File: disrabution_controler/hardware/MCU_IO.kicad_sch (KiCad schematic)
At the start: 48 parts, among them J1 Conn_Coaxial, J2 PROG_PORT, J3 JTAG, Q17 NMOS, U2 ESP32-S2FH2, U3 ECMF02-2AMX6, U9 PI4IOE5V6416LEX, Y1 40 MHz

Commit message: more hardware work
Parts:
- removed R72: 10K, symbol Device:R
- removed R73: 20K, symbol Device:R
- removed TP26: ~, symbol Connector:TestPoint
- added C19, C20, C21, C22: 0uF1, symbol Device:C
- added C23, C24: 10UF, symbol Device:C
- added JP3: ~, symbol Jumper:SolderJumper_3_Open
- added R59, R85: 60R, symbol Device:R
- added U5: TJA1043T, Package_SO:SOIC-14_3.9x8.7mm_P1.27mm, symbol Interface_CAN_LIN:TJA1043T
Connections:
- net +12V: now also C22.1, C24.1, U5.10 (VBAT)
- net +3V3: now also C20.1, C21.1, C23.1, U5.3 (VCC), U5.5 (VIO)
- net CAN_H: now also R59.1, U5.13 (CANH)
- net CAN_L: now also R85.2, U5.12 (CANL)
- net DISRABUTION_NEO_PIXELS: now also U2.28 (GPIO21); no longer U2.37 (GPIO33)
- net GND: now also C19.2, C20.2, C21.2, C22.2, C23.2, C24.2, U5.2 (GND)
- net PERIPHERAL_PWR: now reaches J4.3
- net PERIPHERAL_PWR_GATE: now reaches U2.10 (GPIO5)
- net PERIPHERAL_PWR_CSN_DEV: now reaches U2.18 (GPIO13)
- net CAN_CS renamed CAN_STB
- net CAN_STB: now also U5.14 (~{STB})
- net CAN_INT renamed CAN_ERR
- net CAN_ERR: now also U5.8 (~{ERR})
- net CAN_SCK renamed CAN_RX
- net CAN_RX: now also U5.4 (RXD)
- net CAN_SI renamed CAN_TX
- net CAN_TX: now also U5.1 (TXD)
- net CAN_SO renamed CAN_EN
- net CAN_EN: now also U5.6 (EN)
- new net: JP3.1 (A), R59.2
- new net: C19.1, JP3.2 (C), U5.11 (SPLIT)
- new net: JP3.3 (B), R85.1
- new net CAN_WAKE: U2.37 (GPIO33), U5.9 (WAKE)
- no-connect marks 11 -> 12
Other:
- note removed: "IO EXPANDERS"
- note removed: "IOX_0"
- moved on the sheet: C13, C40, C42, J2, J3, J4, J5, JP1, JP2, Q17, R51, R74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

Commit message: MORE PCB WORK
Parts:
- added D19: S1615-8, Package_SO:SO-16_5.3x10.2mm_P1.27mm, symbol Power_Protection:D3V3X8U9LP3810
- added D20, D21: DT1240A-08LP3810, Package_DFN_QFN:UDFN-9_1.0x3.8mm_P0.5mm, symbol Power_Protection:DT1240A-08LP3810
- added J6, J7, J8: ~, Connector_Phoenix_MC:PhoenixContact_MC_1,5_8-GF-3.81_1x08_P3.81mm_Horizontal_ThreadedFlange, symbol Connector_Generic_MountingPin:Conn_01x08_MountingPin
- C1: renamed from C5; Digikey Part Number (none) -> 399-C0603C104M5RACTUCT-ND
- C10: renamed from C22; footprint (none) -> Capacitor_SMD:C_0603_1608Metric; Digikey Part Number (none) -> 399-C0603C104M5RACTUCT-ND
- C11: renamed from C24; value 10UF -> 10uF; footprint (none) -> Capacitor_SMD:C_0603_1608Metric; Digikey Part Number (none) -> 1276-1038-1-ND
- C12: renamed from C7; Digikey Part Number (none) -> 1276-1038-1-ND
- C13: renamed from C8; Digikey Part Number (none) -> 1276-1038-1-ND
- C14: renamed from C9; Digikey Part Number (none) -> 1276-1038-1-ND
- C15: renamed from C10; Digikey Part Number (none) -> 1276-1038-1-ND
- C16: renamed from C11; Digikey Part Number (none) -> 1276-1038-1-ND
- C17: renamed from C12; Digikey Part Number (none) -> 1276-1038-1-ND
- C18: renamed from C19; footprint (none) -> Capacitor_SMD:C_0603_1608Metric; Digikey Part Number (none) -> 399-C0603C104M5RACTUCT-ND
- C19: renamed from C40; Digikey Part Number (none) -> 1276-1038-1-ND
- C2: renamed from C6; Digikey Part Number (none) -> 399-C0603C104M5RACTUCT-ND
- C20: renamed from C42; value 0.1uF -> 0uF1; Digikey Part Number (none) -> 399-C0603C104M5RACTUCT-ND
- C21: renamed from C15; value 8pF -> 8pF2; Digikey Part Number (none) -> 4713-CHV0603N2508R2BCT-ND
- C22: renamed from C14; value 8pF -> 8pF2; Digikey Part Number (none) -> 4713-CHV0603N2508R2BCT-ND
- C23: renamed from C13; Digikey Part Number (none) -> 399-C0603C104M5RACTUCT-ND
- C3: renamed from C7; Digikey Part Number (none) -> 399-C0603C104M5RACTUCT-ND
- C4: renamed from C8; Digikey Part Number (none) -> 399-C0603C104M5RACTUCT-ND
- C5, C6: Digikey Part Number (none) -> 399-C0603C104M5RACTUCT-ND
- C7: renamed from C23; value 10UF -> 10uF; footprint (none) -> Capacitor_SMD:C_0603_1608Metric; Digikey Part Number (none) -> 1276-1038-1-ND
- C8: renamed from C21; footprint (none) -> Capacitor_SMD:C_0603_1608Metric; Digikey Part Number (none) -> 399-C0603C104M5RACTUCT-ND
- C9: renamed from C20; footprint (none) -> Capacitor_SMD:C_0603_1608Metric; Digikey Part Number (none) -> 399-C0603C104M5RACTUCT-ND
- J1: footprint (none) -> Connector_Coaxial:SMA_Amphenol_132291-12_Vertical; Digikey Part Number (none) -> CONREVSMA001-G-ND
- J2: renamed from J5; footprint CONTROLER:usb4500 -> Library:usb4500; Digikey Part Number (none) -> 2073-USB4500-03-0-ACT-ND
- J4: footprint (none) -> Connector_Dsub:DSUB-9_Pins_Horizontal_P2.77x2.84mm_EdgePinOffset4.94mm_Housed_MountingHolesOffset4.94mm; Digikey Part Number (none) -> AE10921-ND
- JP1: renamed from JP3; footprint (none) -> Jumper:SolderJumper-3_P2.0mm_Open_TrianglePad1.0x1.5mm
- JP2: renamed from JP1; footprint (none) -> Jumper:SolderJumper-2_P1.3mm_Open_TrianglePad1.0x1.5mm
- JP3: renamed from JP2; footprint (none) -> Jumper:SolderJumper-2_P1.3mm_Open_TrianglePad1.0x1.5mm
- Q1: renamed from Q17; footprint (none) -> Resistor_SMD:R_0603_1608Metric; Digikey Part Number (none) -> BSS127H6327XTSA2CT-ND
- R1: renamed from R84; footprint (none) -> Resistor_SMD:R_0603_1608Metric; Digikey Part Number (none) -> 541-1.00KHCT-ND
- R10: renamed from R74; Digikey Part Number (none) -> 541-4030-1-ND
- R11: renamed from R78; footprint (none) -> Resistor_SMD:R_0603_1608Metric; Digikey Part Number (none) -> RMCF0603JT10K0CT-ND
- R12: renamed from R77; footprint (none) -> Resistor_SMD:R_0603_1608Metric; Digikey Part Number (none) -> RMCF0603JT10K0CT-ND
- R2: renamed from R50; footprint (none) -> Resistor_SMD:R_0603_1608Metric; Digikey Part Number (none) -> 541-1.00KHCT-ND
- R3: renamed from R2; Digikey Part Number (none) -> RMCF0603JT10K0CT-ND
- R4: renamed from R59; value 60R -> 60R4; footprint (none) -> Resistor_SMD:R_0603_1608Metric; Digikey Part Number (none) -> 541-5507-1-ND
- R5: renamed from R85; value 60R -> 60R4; footprint (none) -> Resistor_SMD:R_0603_1608Metric; Digikey Part Number (none) -> 541-5507-1-ND
- R6: renamed from R5; Digikey Part Number (none) -> RMCF0603JT10K0CT-ND
- R7: renamed from R51; Digikey Part Number (none) -> RMCF0603JT10K0CT-ND
- R8: renamed from R76; Digikey Part Number (none) -> 541-4026-1-ND
- R9: renamed from R75; Digikey Part Number (none) -> 541-4030-1-ND
- TP1: renamed from TP28; footprint (none) -> TestPoint:TestPoint_Pad_D1.0mm; now left out of the parts list
- TP2: renamed from TP27; footprint (none) -> TestPoint:TestPoint_Pad_D1.0mm; now left out of the parts list
- TP3: renamed from TP25; footprint (none) -> TestPoint:TestPoint_Pad_D1.0mm; now left out of the parts list
- TP4: renamed from TP24; footprint (none) -> TestPoint:TestPoint_Pad_D1.0mm; now left out of the parts list
- TP5: renamed from TP15; now left out of the parts list
- TP6: renamed from TP29; footprint (none) -> TestPoint:TestPoint_Pad_D1.0mm; now left out of the parts list
- U1: renamed from U5; value TJA1043T -> TJA1043T/1J; Digikey Part Number (none) -> 568-13274-1-ND
- U2: Digikey Part Number (none) -> 1904-ESP32-S2FH2CT-ND
- U3: renamed from U9; footprint PCM_Package_SO_AKL:TSSOP-24_4.4x7.8mm_P0.65mm -> Package_SO:TSSOP-24_4.4x7.8mm_P0.65mm; Digikey Part Number (none) -> PI4IOE5V6416LEXDICT-ND
- U4: renamed from U3; Digikey Part Number (none) -> 497-10773-1-ND
- Y1: footprint CONTROLER:cx3225sa_e -> Library:cx3225sa_e; Digikey Part Number (none) -> 478-CX3225SA40000D0PTWCCCT-ND
- renumbered J2 to J5
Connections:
- net ALLOW_Q_DRAW: now also D19.2 (Line-3)
- net CAN_H: now also D19.7 (Line-4), J6.6 (Pin_6)
- net CAN_L: now also D19.8 (Line-2), J6.5 (Pin_5)
- net CH10_GATE: now also U3.19 (P1_6); no longer U3.14 (P1_1)
- net CH11_GATE: now also U3.18 (P1_5); no longer U3.15 (P1_2)
- net CH12_GATE: now also U3.17 (P1_4); no longer U3.16 (P1_3)
- net CH13_GATE: now also U3.16 (P1_3); no longer U3.17 (P1_4)
- net CH14_GATE: now also U3.15 (P1_2); no longer U3.18 (P1_5)
- net CH15_GATE: now also U3.14 (P1_1); no longer U3.19 (P1_6)
- net CH16_GATE: now also U3.13 (P1_0); no longer U3.20 (P1_7), U3.4 (P0_0)
- net CH2_GATE: now also U3.10 (P0_6); no longer U3.5 (P0_1)
- net CH3_GATE: now also U3.9 (P0_5); no longer U3.6 (P0_2)
- net CH4_GATE: now also U3.8 (P0_4); no longer U3.7 (P0_3)
- net CH5_GATE: now also U3.7 (P0_3); no longer U3.8 (P0_4)
- net CH6_GATE: now also U3.6 (P0_2); no longer U3.9 (P0_5)
- net CH7_GATE: now also U3.5 (P0_1); no longer U3.10 (P0_6)
- net CH8_GATE: now also U3.4 (P0_0); no longer U3.11 (P0_7)
- net CH9_GATE: now also U3.20 (P1_7); no longer U3.13 (P1_0)
- net ESP_RX: now also D20.5 (K4), J6.1 (Pin_1)
- net ESP_TX: now also D20.4 (K3), J6.2 (Pin_2)
- net GND: now also D19.10 (Line-4), D19.11, D19.12 (Line-7), D19.13 (Line-8), D19.14 (Line-6), D19.15 (Line-3), D19.16 (Line-1), D19.9 (Line-2), D20.3 (A), D21.3 (A), J6.8 (Pin_8), J7.8 (Pin_8), J8.7 (Pin_7)
- net I2C_SCL: now also D20.2 (K2), J6.3 (Pin_3)
- net I2C_SDA: now also D20.1 (K1), J6.4 (Pin_4)
- net PERIPHERAL_PWR: now also D19.3 (Line-6), D19.4 (Line-8), D19.5 (Line-7), D19.6 (Line-5), J6.7 (Pin_7), J7.7 (Pin_7), J8.8 (Pin_8)
- net CAR_ACC_ESD: now reaches J4.9, Q1.2 (G), R12.1
- net CAR_ACC_ESD: now also D19.1 (Line-1)
- net GPIO6: now reaches U2.11 (GPIO6)
- net GPIO6: now also D21.7 (K6), J7.6 (Pin_6)
- net GPIO7: now reaches U2.12 (GPIO7)
- net GPIO7: now also D21.6 (K5), J7.5 (Pin_5)
- net GPIO8: now reaches U2.13 (GPIO8)
- net GPIO8: now also D21.5 (K4), J7.4 (Pin_4)
- net GPIO9: now reaches U2.14 (GPIO9)
- net GPIO9: now also D21.4 (K3), J7.3 (Pin_3)
- net GPIO10: now reaches U2.15 (GPIO10)
- net GPIO10: now also D21.2 (K2), J7.2 (Pin_2)
- net GPIO11: now reaches U2.16 (GPIO11)
- net GPIO11: now also D21.1 (K1), J7.1 (Pin_1)
- net GPIO12: now reaches U2.17 (GPIO12)
- net GPIO12: now also D20.7 (K6), J8.4 (Pin_4)
- net ADC_01_ALERT: now reaches U2.21 (XTAL_32K_P)
- net ADC_02_ALERT: now reaches U2.22 (XTAL_32K_N)
- net DAC_1: now reaches U2.23 (DAC_1)
- net DAC_1: now also D21.9 (K8), J8.5 (Pin_5)
- net DAC_2: now reaches U2.24 (DAC_2)
- net DAC_2: now also D21.8 (K7), J8.6 (Pin_6)
- new net CH1_GATE: U3.11 (P0_7)
- no-connect marks 12 -> 13
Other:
- moved on the sheet: C21, C22, Y1

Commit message: more hardware work on disrabution controler nearing ifc
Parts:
- C1, C2, C23, C3, C4, C5, C6: DIGIKEY PART # 399-C0603C104M5RACTUCT-ND -> (none)
- C12, C13, C14, C15, C16, C17: DIGIKEY PART # 1276-1038-1-ND -> (none)
- C21, C22: DIGIKEY PART # 4713-CHV0603N2508R2BCT-ND -> (none)
- D19: DIGIKEY PART NUMBER 1655-S1615-8CT-ND -> (none)
- D20, D21: DIGIKEY PART NUMBER DT1240A-08LP3810-7DICT-ND -> (none)
- J2: DIGIKEY PART # 2073-USB4500-03-0-ACT-ND -> (none)
- J6, J7, J8: DIGIKEY PART NUMBER 609-3825-ND -> (none)
- Q1: footprint Resistor_SMD:R_0603_1608Metric -> Package_TO_SOT_SMD:SOT-23
- R10, R9: DIGIKEY PART # 541-4030-1-ND -> (none)
- R3, R6: DIGIKEY PART # RMCF0603JT10K0CT-ND -> (none)
- R8: DIGIKEY PART # 541-4026-1-ND -> (none)
- U2: DIGIKEY PART # 1904-ESP32-S2FH2CT-ND -> (none)
- U4: DIGIKEY PART # 497-10773-1-ND -> (none)
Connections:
- net CAN_EN: now also U2.42 (GPIO38); no longer U2.40 (GPIO36)
- net CAN_ERR: now also U2.37 (GPIO33); no longer U2.38 (GPIO34)
- net CAN_TX: now also U2.40 (GPIO36); no longer U2.42 (GPIO38)
- net CAN_WAKE: now also U2.38 (GPIO34); no longer U2.37 (GPIO33)
- net CAR_ACC: now also Q1.3 (D); no longer Q1.1 (D)
- net CAR_ACC_ESD: now also Q1.1 (G); no longer Q1.2 (G)
- net DAC_1: now also D21.6 (K5); no longer D21.9 (K8)
- net DAC_2: now also D21.5 (K4); no longer D21.8 (K7)
- net ESP_IO0: now also D20.8 (K7)
- net ESP_RX: now also D20.6 (K5); no longer D20.5 (K4)
- net GND: now also Q1.2 (S); no longer Q1.3 (S)
- net GPIO10: now also D21.7 (K6); no longer D21.2 (K2)
- net GPIO11: now also D21.4 (K3); no longer D21.1 (K1)
- net GPIO12: now also D20.5 (K4); no longer D20.7 (K6)
- net GPIO6: now also D21.1 (K1); no longer D21.7 (K6)
- net GPIO7: now also D21.9 (K8); no longer D21.6 (K5)
- net GPIO8: now also D21.2 (K2); no longer D21.5 (K4)
- net GPIO9: now also D21.8 (K7); no longer D21.4 (K3)
- net RST: now also D20.7 (K6)
- net LNA: now reaches J1.1 (In), U2.2 (LNA_IN)
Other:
- moved on the sheet: J7

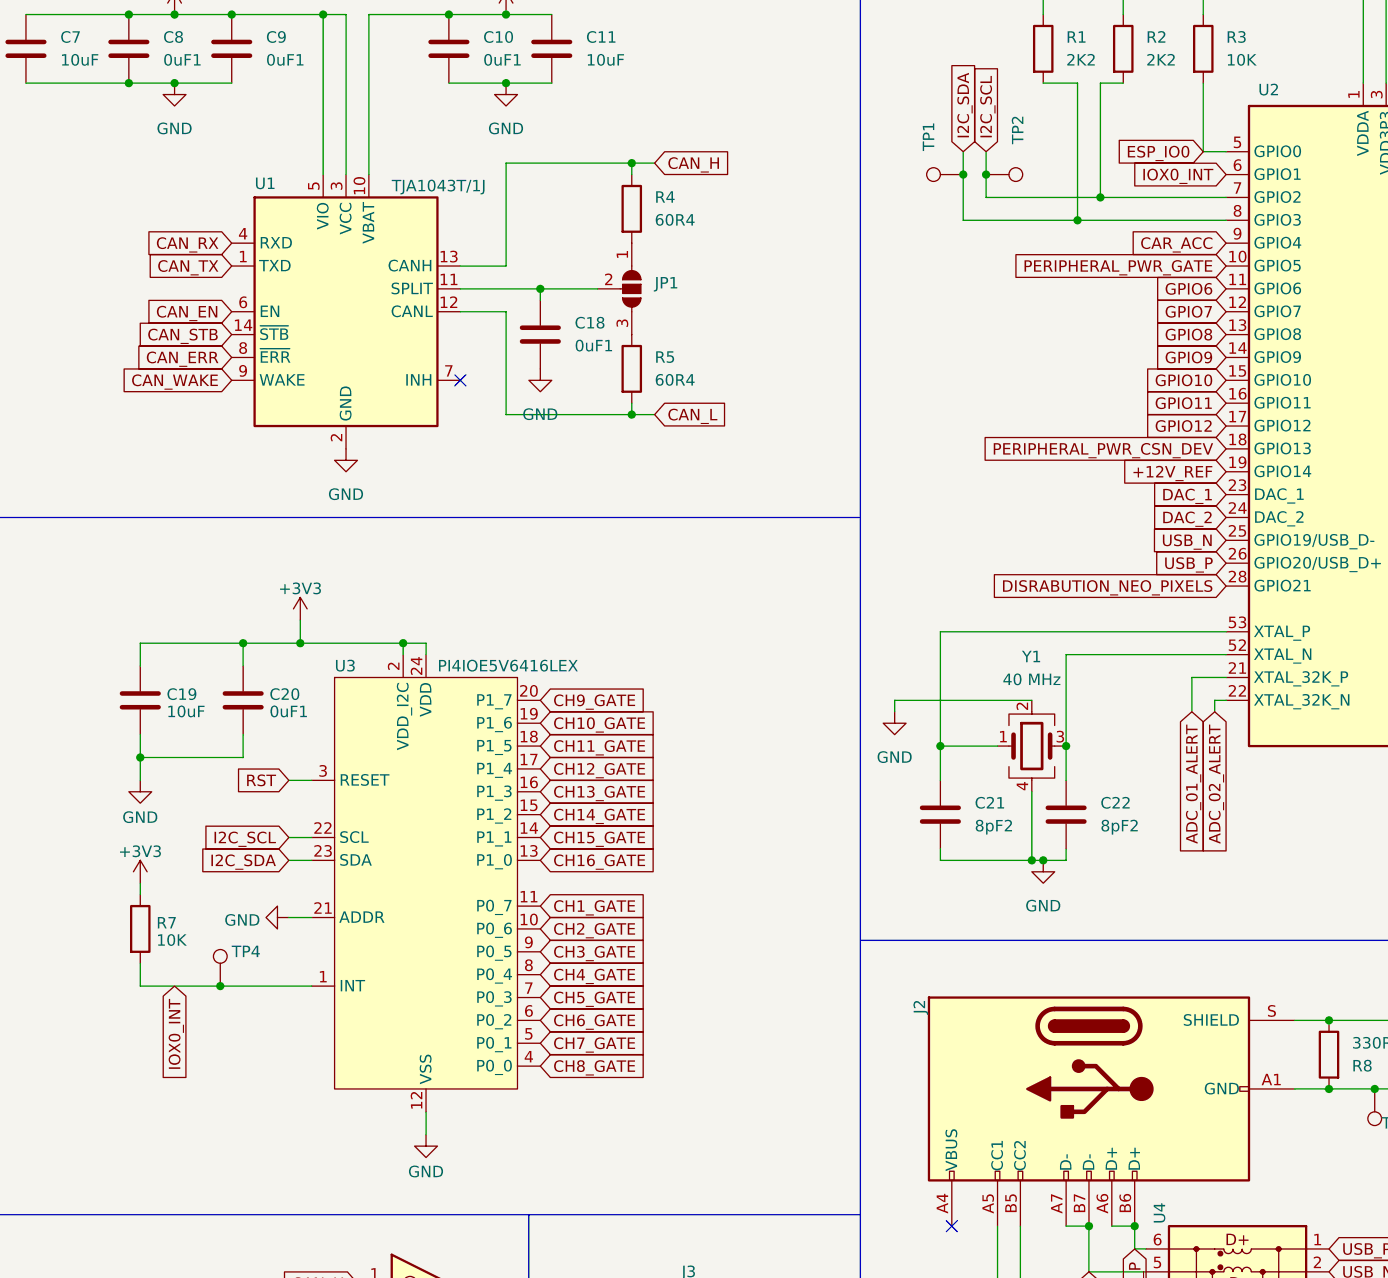
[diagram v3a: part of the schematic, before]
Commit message: working on firmware but notaced a hardware issue
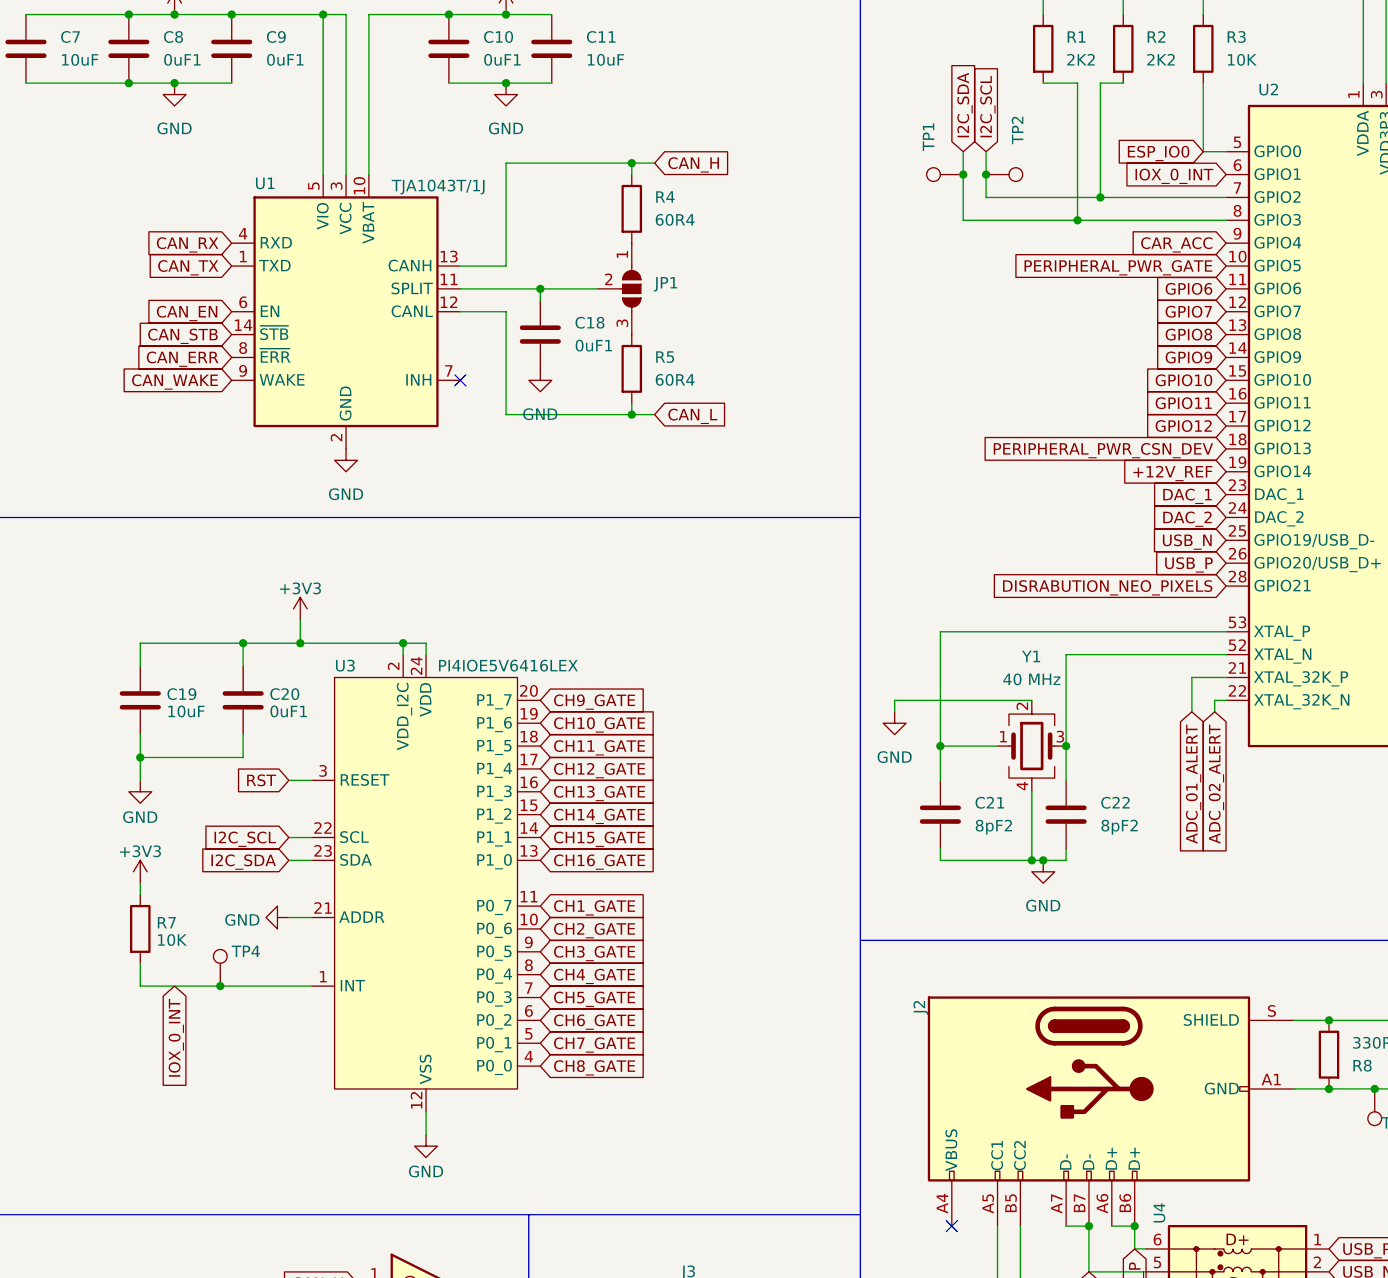
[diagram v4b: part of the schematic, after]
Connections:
- net IOX0_INT renamed IOX_0_INT
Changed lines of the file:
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@@
 		)
 	)
-	(global_label "IOX0_INT"
+	(global_label "IOX_0_INT"
 		(shape input)
 		(at 34.29 129.54 270)
@@
 		)
 		(property "Intersheetrefs" "${INTERSHEET_REFS}"
-			(at 34.29 140.75 90)
+			(at 34.29 141.7176 90)
 			(effects
 				(font
@@
 		)
 	)
-	(global_label "IOX0_INT"
+	(global_label "IOX_0_INT"
 		(shape input)
 		(at 151.13 39.37 180)
@@
 		)
 		(property "Intersheetrefs" "${INTERSHEET_REFS}"
-			(at 139.9994 39.37 0)
-			(effects
-				(font
+			(at 138.9524 39.37 0)
+			(effects
+				(font

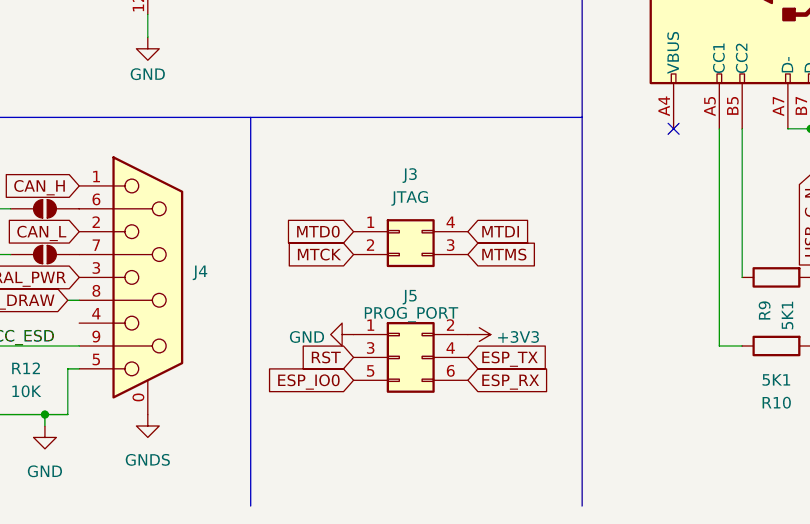
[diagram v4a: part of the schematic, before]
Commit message: changed programing headder
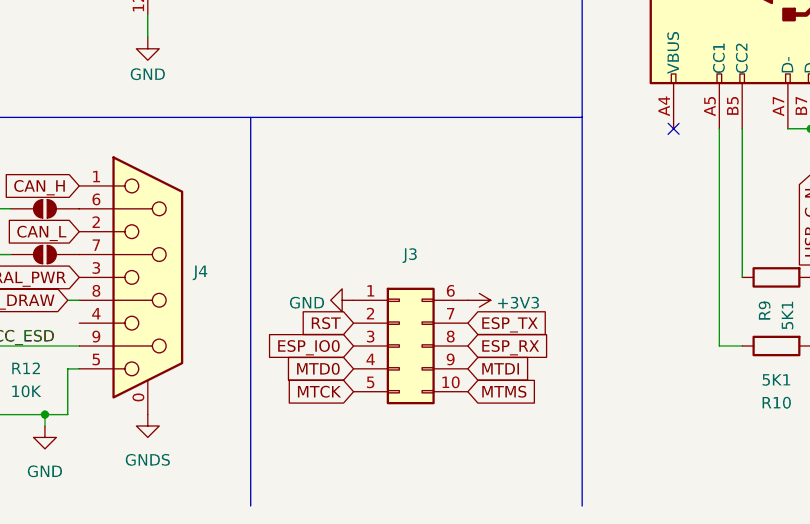
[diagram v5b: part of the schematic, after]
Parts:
- removed J3: JTAG, Connector_PinHeader_2.54mm:PinHeader_2x02_P2.54mm_Vertical, symbol Connector_Generic:Conn_02x02_Counter_Clockwise
- removed J5: PROG_PORT, Connector_PinHeader_2.54mm:PinHeader_2x03_P2.54mm_Vertical, symbol Connector_Generic:Conn_02x03_Odd_Even
- added J3: ~, Connector_PinHeader_2.54mm:PinHeader_2x05_P2.54mm_Vertical, symbol Connector_Generic:Conn_02x05_Top_Bottom
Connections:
- net +3V3: now also J3.6 (Pin_6)
- net ESP_IO0: now also J3.3 (Pin_3)
- net ESP_RX: now also J3.8 (Pin_8)
- net ESP_TX: now also J3.7 (Pin_7)
- net GND: now also J3.1 (Pin_1)
- net MTCK: now also J3.5 (Pin_5)
- net MTD0: now also J3.4 (Pin_4)
- net MTDI: now also J3.9 (Pin_9)
- net MTMS: now also J3.10 (Pin_10)
- net RST: now also J3.2 (Pin_2)
